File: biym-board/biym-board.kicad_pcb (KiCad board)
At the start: 2 copper layers, 50.8 x 34 mm, 7 parts, among them J1 JST_SH_BM02_VERTICAL, Q1 MOSFET-N-CH-EN, Q2 MOSFET-P-CH-EN

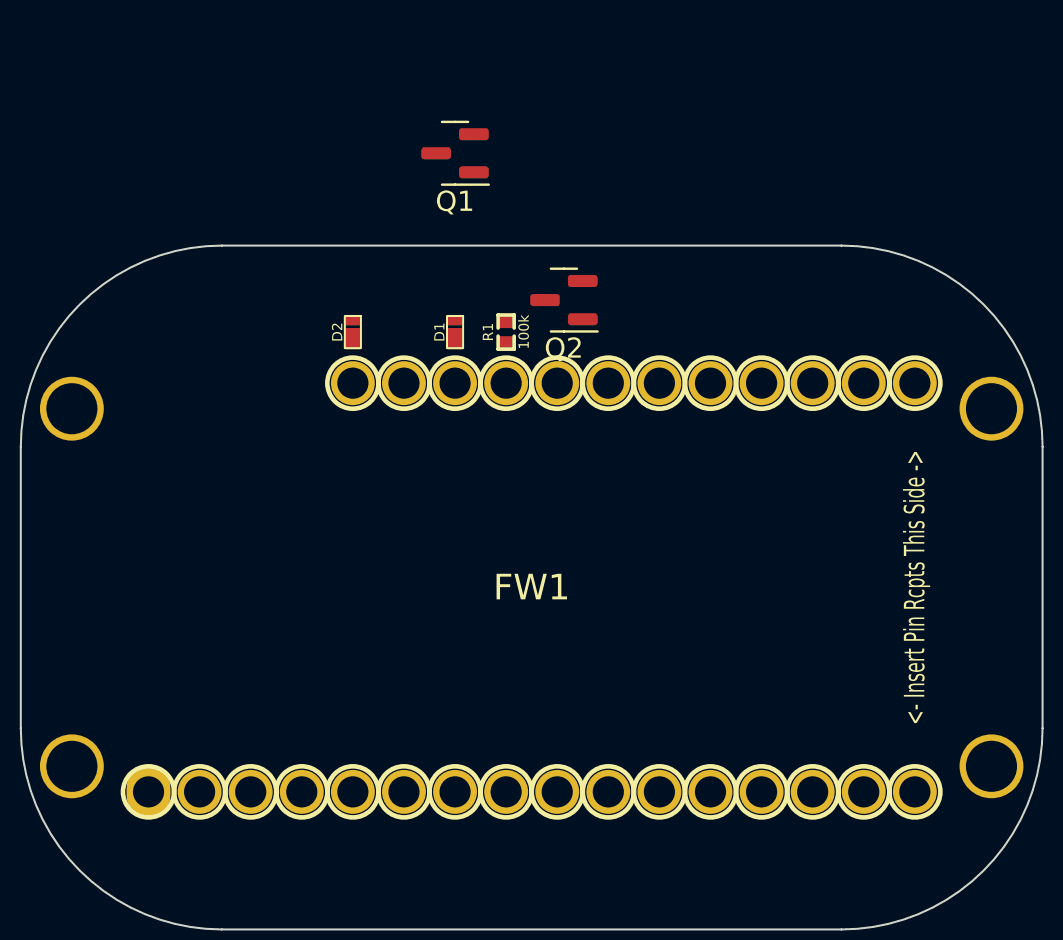
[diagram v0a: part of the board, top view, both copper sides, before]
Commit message: Switch feather contacts to pogo pins
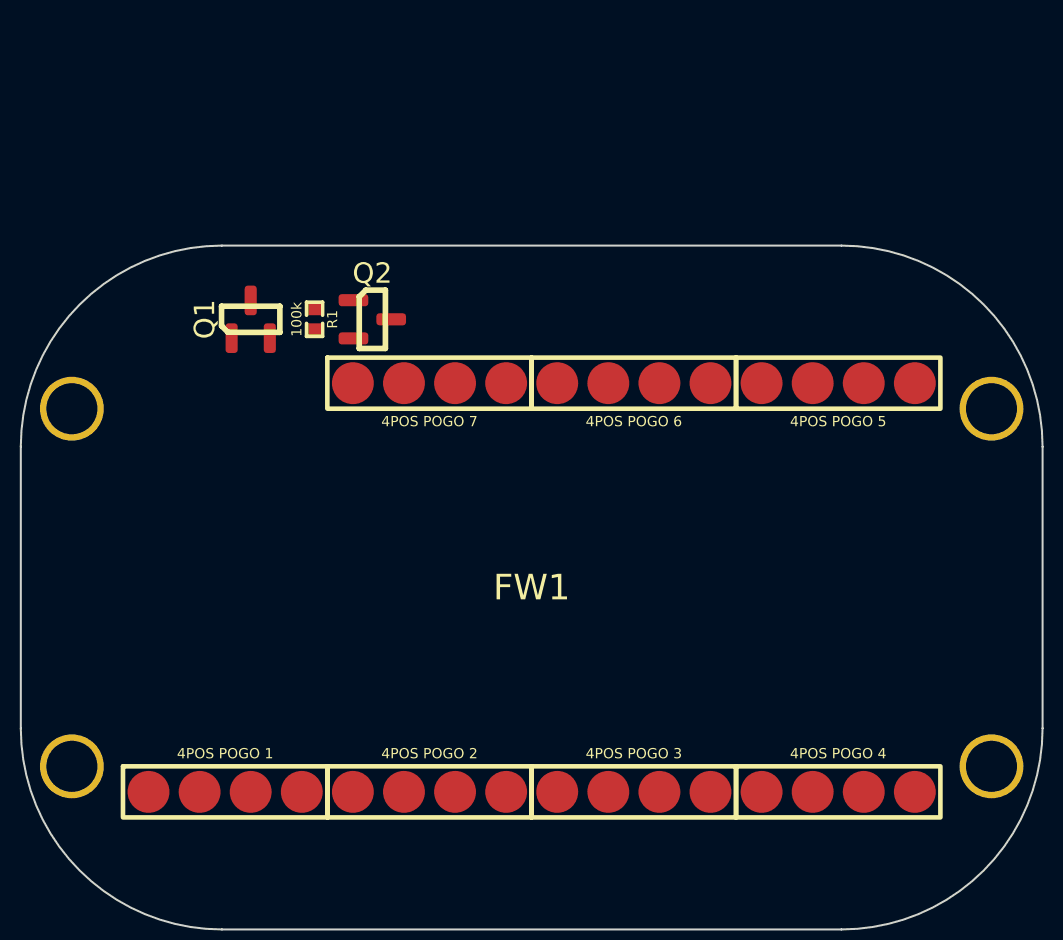
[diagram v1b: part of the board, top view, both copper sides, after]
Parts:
- removed D1, D2: DIODE_SCHOTTKY_40V_2A_0603, Janelia:SM0603_DSN2
- FW1: value FEATHERWING_nRF52_PIN_RECEPTACLES -> FEATHERWING_nRF52_POGO_PINS; footprint Janelia:FEATHERWING_PIN_RECEPTACLES -> Janelia:FEATHERWING_POGO_PINS
- moved Q1 13.1 mm to (126.0, 86.7), turned to 90 degrees
- moved Q2 9.57 mm to (132.1, 86.7), turned to 0 degrees
- moved R1 9.55 mm to (129.2, 86.7), turned to 0 degrees
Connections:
- net /ENABLE_VCC renamed /ENABLE_PERIPHERAL_POWER
- net /power/VCC renamed /power/VPERIPHERAL
- net /power/~{ENABLE_VCC} renamed /power/~{ENABLE_PERIPHERAL_POWER}
- FW1 pad 26: /VUSB -> unconnected-(FW1-Pad26)
- FW1 pad 28: /VBAT -> /VBATTERY
- Q2 pad 2: /power/VAA -> /VBATTERY
- R1 pad 2: /power/VAA -> /VBATTERY

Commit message: Add driver external components
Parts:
- added J2: HEADER_01X03_JST_PH_VERTICAL, Janelia:JST_PH_B3B-PH-K_1x03_P2.00mm_Vertical, F.Cu at (123.5, 122.9)
- added U1: DRV8311H, Janelia:WQFN-24-1EP_3x3mm_P0.4mm_EP1.9x1.9mm_ThermalVias, F.Cu at (133.0, 122.7)
- J1: value JST_SH_BM02_VERTICAL -> HEADER_01X02_JST_SH_SMD_VERTICAL
- moved J1 37.5 mm to (134.9, 86.0), turned to 0 degrees
- moved Q1 14.1 mm to (137.5, 94.9), turned to -90 degrees
- moved R1 9.38 mm to (133.7, 94.9), turned to 180 degrees
- moved Q2 8.55 mm to (129.8, 94.9), turned to 180 degrees
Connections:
- FW1 pad 2: unconnected-(FW1-Pad2) -> /VDIGITAL
- Q2 pad 3: /power/VPERIPHERAL -> /VPERIPHERAL

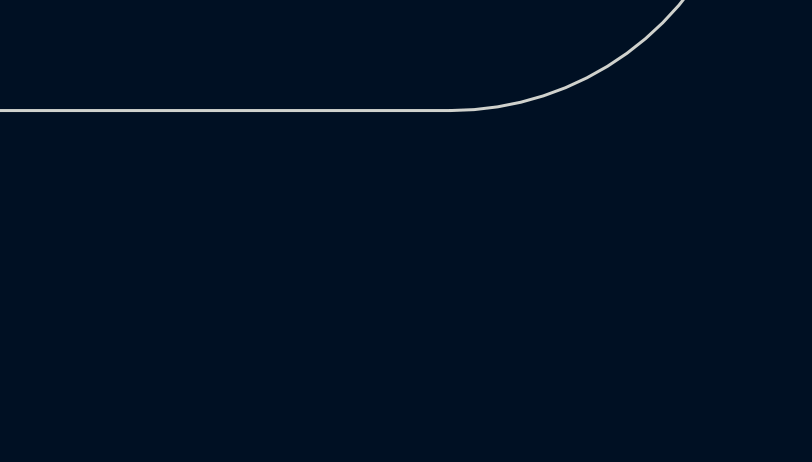
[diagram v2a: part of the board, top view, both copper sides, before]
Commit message: Add motor feedback
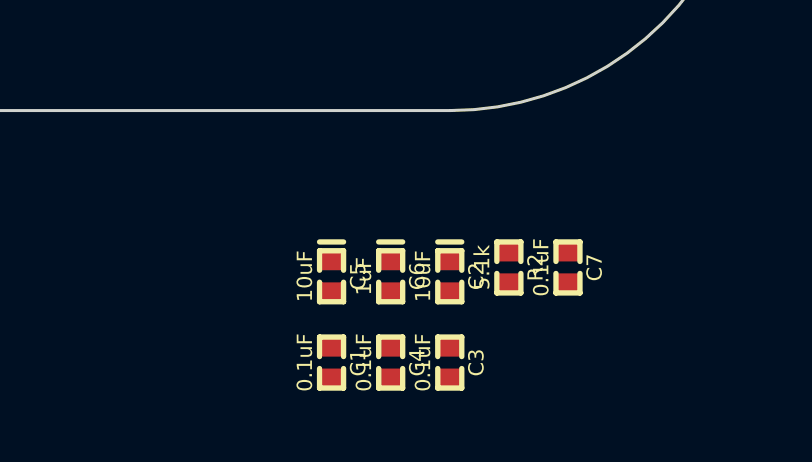
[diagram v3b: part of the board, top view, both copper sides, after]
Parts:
- added C1: 0.1uF, Janelia:SM0402, F.Cu at (151.4, 125.4)
- added C2: 10uF, Janelia:SM0402_POL, F.Cu at (155.4, 122.5)
- added C3: 0.1uF, Janelia:SM0402, F.Cu at (155.4, 125.4)
- added C4: 0.1uF, Janelia:SM0402, F.Cu at (153.4, 125.4)
- added C5: 10uF, Janelia:SM0402_POL, F.Cu at (151.4, 122.5)
- added C6: 1uF, Janelia:SM0402_POL, F.Cu at (153.4, 122.5)
- added C7: 0.1uF, Janelia:SM0402, F.Cu at (159.3, 122.2)
- added R2: 5.1k, Janelia:SM0402, F.Cu at (157.3, 122.2)
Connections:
- FW1 pad 20: unconnected-(FW1-Pad20) -> /~{DRIVER_FAULT}
- FW1 pad 21: unconnected-(FW1-Pad21) -> /~{DRIVER_SLEEP}
- FW1 pad 22: unconnected-(FW1-Pad22) -> /DRIVER_PWM_A
- FW1 pad 23: unconnected-(FW1-Pad23) -> /DRIVER_PWM_B
- FW1 pad 24: unconnected-(FW1-Pad24) -> /DRIVER_PWM_C
- U1 pad 1: /motor_driver/~{FAULT} -> /~{DRIVER_FAULT}
- U1 pad 13: /motor_driver/PWM_C -> /DRIVER_PWM_C
- U1 pad 14: /motor_driver/PWM_B -> /DRIVER_PWM_B
- U1 pad 15: /motor_driver/PWM_A -> /DRIVER_PWM_A
- U1 pad 24: /motor_driver/~{SLEEP} -> /~{DRIVER_SLEEP}

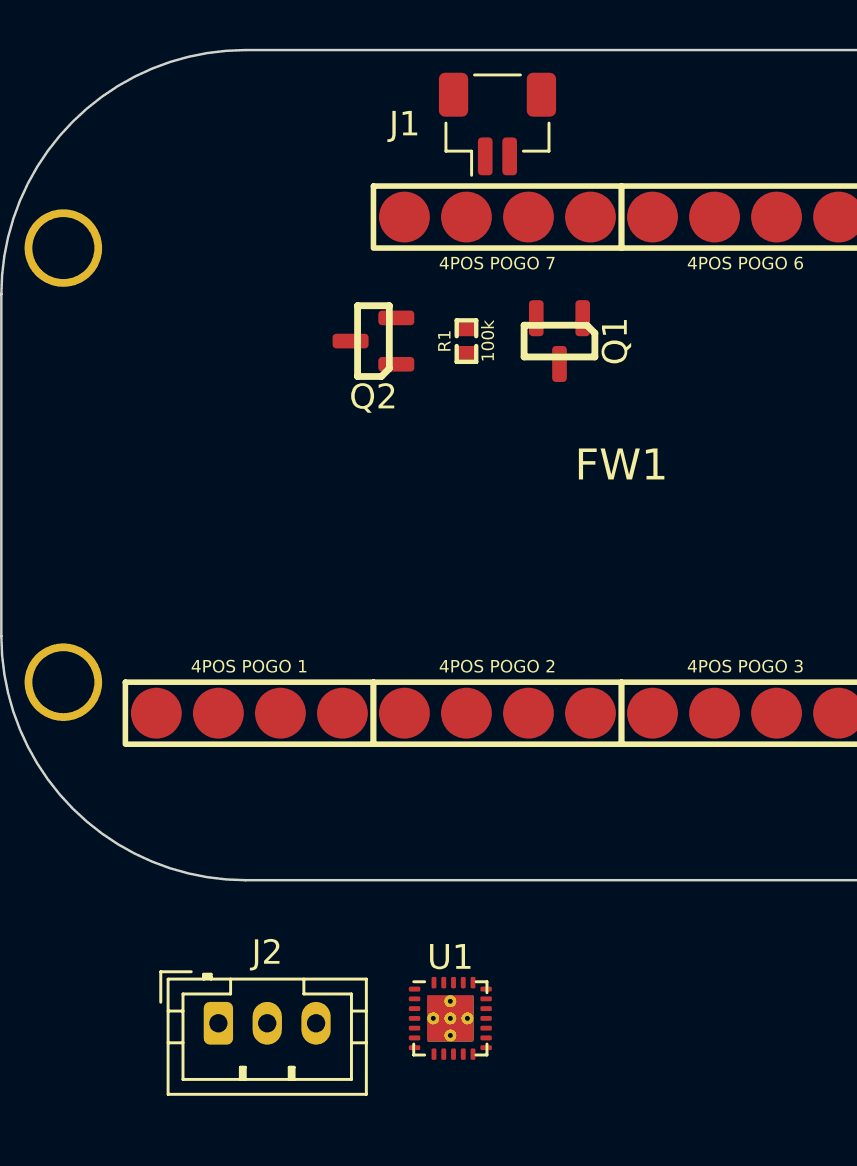
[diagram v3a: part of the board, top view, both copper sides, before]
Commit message: Rename sheets
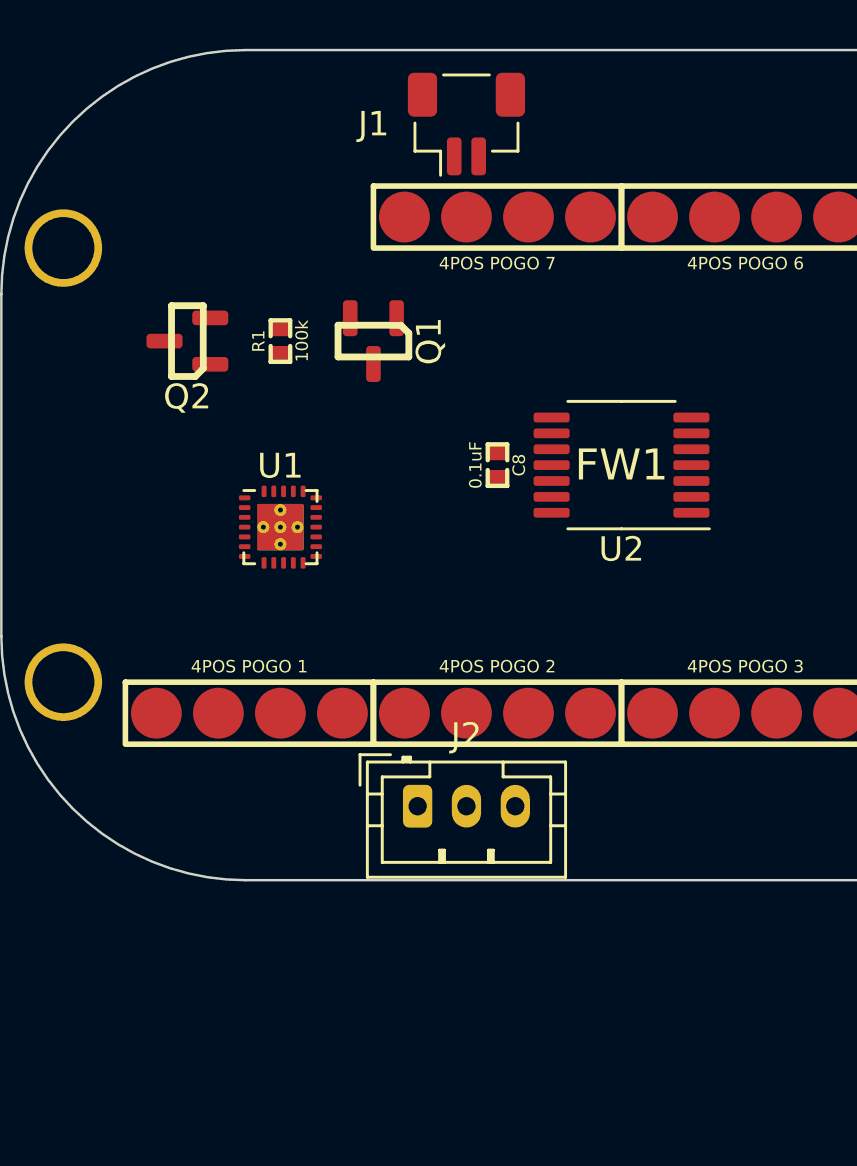
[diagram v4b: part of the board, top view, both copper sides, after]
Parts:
- added C8: 0.1uF, Janelia:SM0402, F.Cu at (134.9, 100.0)
- added U2: AS5047P, Janelia:TSSOP-14_4.4x5mm_P0.65mm, F.Cu at (140.0, 100.0)
- moved U1 21.3 mm to (126.0, 102.5)
- moved J2 13.5 mm to (133.7, 114.0)
- moved Q1 7.62 mm to (129.8, 94.9)
- moved Q2 7.62 mm to (122.2, 94.9)
- moved R1 7.62 mm to (126.0, 94.9)
- moved J1 1.27 mm to (133.7, 86.0)
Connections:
- net /motor_driver/CP renamed /driver/CP
- net /motor_driver/CSAREF renamed /driver/CSAREF
- net /motor_driver/MOTOR_A renamed /driver/MOTOR_A
- net /motor_driver/MOTOR_B renamed /driver/MOTOR_B
- net /motor_driver/MOTOR_C renamed /driver/MOTOR_C
- net /motor_driver/VDD renamed /driver/VDD
- FW1 pad 10: unconnected-(FW1-Pad10) -> /~{ENCODER_CS}
- FW1 pad 11: unconnected-(FW1-Pad11) -> /SCK
- FW1 pad 12: unconnected-(FW1-Pad12) -> /MOSI
- FW1 pad 13: unconnected-(FW1-Pad13) -> /MISO
- FW1 pad 5: unconnected-(FW1-Pad5) -> /ENCODER_A
- FW1 pad 6: unconnected-(FW1-Pad6) -> /ENCODER_B

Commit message: Finished v0.1 of schematic
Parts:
- added C10: C_0.1uF_0402, Janelia:SM0402, F.Cu at (213.7, 102.9)
- added C11: C_0.1uF_0402, Janelia:SM0402, F.Cu at (210.3, 92.7)
- added C12: C_0.1uF_0402, Janelia:SM0402, F.Cu at (190.0, 110.0)
- added C13: C_10uF_0402_POL, Janelia:SM0402_POL, F.Cu at (190.0, 107.1)
- added C14: C_0.1uF_0402, Janelia:SM0402, F.Cu at (184.3, 99.0)
- added C15: C_0.1uF_0402, Janelia:SM0402, F.Cu at (186.2, 99.0)
- added C9: C_1uF_0402_POL, Janelia:SM0402_POL, F.Cu at (211.8, 103.2)
- added J3: HEADER_01X04_JST_ZH_SMD_VERTICAL, Janelia:JST_ZH_B4B_ZR_SM4_TF_1x04-1MP_P1.50mm_Vertical, F.Cu at (183.4, 108.2)
- added J4: HEADER_01X03_JST_ZH_SMD_VERTICAL, Janelia:JST_ZH_B3B_ZR_SM4_TF_1x03-1MP_P1.50mm_Vertical, F.Cu at (192.3, 94.1)
- added J5: HEADER_01X03_JST_ZH_SMD_VERTICAL, Janelia:JST_ZH_B3B_ZR_SM4_TF_1x03-1MP_P1.50mm_Vertical, F.Cu at (182.7, 94.1)
- added J6: HEADER_01X03_JST_ZH_SMD_VERTICAL, Janelia:JST_ZH_B3B_ZR_SM4_TF_1x03-1MP_P1.50mm_Vertical, F.Cu at (200.1, 108.2)
- added L1: 2.2uH, Janelia:INDUCTOR_VLS_HBX, F.Cu at (218.9, 93.5)
- added U3: AS5047P, Janelia:TSSOP-14_4.4x5mm_P0.65mm, F.Cu at (205.0, 94.6)
- added U4: LT_SN74LVC2T45DCUT, Janelia:VSSOP-8_2.4x2.1mm_P0.5mm, F.Cu at (180.6, 99.4)
- C1, C3: value 0.1uF -> C_10uF_0603; footprint Janelia:SM0402 -> Janelia:SM0603
- C2: value 10uF -> C_10uF_0603; footprint Janelia:SM0402_POL -> Janelia:SM0603
- C4, C8: value 0.1uF -> C_0.1uF_0402
- C5: value 10uF -> C_0.1uF_0402; footprint Janelia:SM0402_POL -> Janelia:SM0402
- C6: value 1uF -> C_10uF_0402_POL
- C7: value 0.1uF -> C_10uF_0402_POL; footprint Janelia:SM0402 -> Janelia:SM0402_POL
- J2: value HEADER_01X03_JST_PH_VERTICAL -> HEADER_01X03_JST_ZH_SMD_VERTICAL; footprint Janelia:JST_PH_B3B-PH-K_1x03_P2.00mm_Vertical -> Janelia:JST_ZH_B3B_ZR_SM4_TF_1x03-1MP_P1.50mm_Vertical
- R1: value 100k -> R_110k_0402
- R2: value 5.1k -> R_5.1k_0402
- U1: value DRV8311H -> BOOST_5V_RP402N501F; footprint Janelia:WQFN-24-1EP_3x3mm_P0.4mm_EP1.9x1.9mm_ThermalVias -> Janelia:SOT-23-5
- U2: value AS5047P -> DRV8311H; footprint Janelia:TSSOP-14_4.4x5mm_P0.65mm -> Janelia:WQFN-24-1EP_3x3mm_P0.4mm_EP1.9x1.9mm_ThermalVias
- moved C8 50.0 mm to (181.9, 82.9)
- turned R1 to 0 degrees
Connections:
- C1 pad 1: /VPERIPHERAL -> /VBATTERY
- C2 pad 1: /VPERIPHERAL -> /VBOOSTED
- C3 pad 1: /VPERIPHERAL -> /VBOOSTED
- C3 pad 2: /driver/CP -> /GND
- C4 pad 1: /VDIGITAL -> /VPERIPHERAL
- C6 pad 1: /driver/VDD -> /VPERIPHERAL
- C7 pad 1: /driver/CSAREF -> /VDIGITAL
- C8 pad 1: /VDIGITAL -> /VPERIPHERAL
- C8 pad 2: /GND -> /driver/CP
- FW1 pad 19: unconnected-(FW1-Pad19) -> /GPIO_0
- FW1 pad 20: /~{DRIVER_FAULT} -> /GPIO_1
- FW1 pad 21: /~{DRIVER_SLEEP} -> /SERVO_SIGNAL_0
- FW1 pad 22: /DRIVER_PWM_A -> /SERVO_SIGNAL_1
- FW1 pad 23: /DRIVER_PWM_B -> /DRIVER_PWM_A
- FW1 pad 24: /DRIVER_PWM_C -> /DRIVER_PWM_B
- FW1 pad 25: /ENABLE_PERIPHERAL_POWER -> /DRIVER_PWM_C
- FW1 pad 3: unconnected-(FW1-Pad3) -> /ENABLE_PERIPHERAL_POWER
- FW1 pad 7: unconnected-(FW1-Pad7) -> /ENABLE_BOOSTED_POWER
- FW1 pad 8: unconnected-(FW1-Pad8) -> /~{DRIVER_FAULT}
- FW1 pad 9: unconnected-(FW1-Pad9) -> /~{DRIVER_SLEEP}
- Q1 pad 3: /power/~{ENABLE_PERIPHERAL_POWER} -> /power/~{ENABLE_PERIPHERAL}
- Q2 pad 1: /power/~{ENABLE_PERIPHERAL_POWER} -> /power/~{ENABLE_PERIPHERAL}
- R1 pad 1: /power/~{ENABLE_PERIPHERAL_POWER} -> /VBATTERY
- R1 pad 2: /VBATTERY -> /power/~{ENABLE_PERIPHERAL}
- U1 pad 1: /~{DRIVER_FAULT} -> /power/LX
- U1 pad 2: /driver/CSAREF -> /GND
- U1 pad 3: unconnected-(U1-Pad3) -> /ENABLE_BOOSTED_POWER
- U1 pad 4: unconnected-(U1-Pad4) -> /VBATTERY
- U1 pad 5: unconnected-(U1-Pad5) -> /VBOOSTED
- U2 pad 1: /~{ENCODER_CS} -> /~{DRIVER_FAULT}
- U2 pad 10: unconnected-(U2-Pad10) -> /driver/MOTOR_A
- U2 pad 11: /VDIGITAL -> /driver/MOTOR_B
- U2 pad 12: /VDIGITAL -> /driver/MOTOR_C
- U2 pad 13: /GND -> /DRIVER_PWM_C
- U2 pad 14: unconnected-(U2-Pad14) -> /DRIVER_PWM_B
- U2 pad 2: /SCK -> /driver/CSAREF
- U2 pad 3: /MOSI -> unconnected-(U2-Pad3)
- U2 pad 4: /MISO -> unconnected-(U2-Pad4)
- U2 pad 5: /GND -> unconnected-(U2-Pad5)
- U2 pad 6: /ENCODER_B -> /driver/CP
- U2 pad 7: /ENCODER_A -> /VDIGITAL
- U2 pad 8: unconnected-(U2-Pad8) -> /VPERIPHERAL
- U2 pad 9: unconnected-(U2-Pad9) -> /GND
